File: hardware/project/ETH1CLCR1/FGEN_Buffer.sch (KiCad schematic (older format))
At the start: 37 parts, among them K1201 UMS05-1A80-75D, K1202 UMS05-1A80-75D, K1203 UMS05-1A80-75D, K1204 UMS05-1A80-75D, Q1201 MMBT4401L, Q1202 MMBT4403L, U1201 LT1468

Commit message: Schematic design
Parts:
- added C1205, C1206, C1207, C1208: 100n, symbol Device:C
- added C1209: C, symbol Device:C
- added R1219, R1220: R, symbol Device:R
- added U1202: TL072, symbol Amplifier_Operational:TL072
- gave numbers to parts that had none: 18
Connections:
- net +15VF: now also C1205.1, C1206.1, U1202.8 (V+)
- net -15VF: now also C1207.1, C1208.1, U1202.4 (V-)
- net AGNDF: now also C1205.2, C1206.2, C1207.2, C1208.2, U1202.3 (+), U1202.5 (+)
- net FGEN: now reaches U1201.3 (+)
- net at R1204.1, R1206.1, R1213.1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: now also R1219.2, U1202.2 (-)
- net SR10KCTR: now reaches R1209.1
- net SR1KCTR: now reaches R1210.1
- net SR100CTR: now reaches R1211.1
- net SR10CTR: now reaches R1212.1
- new net: C1209.2, R1219.1, U1202.1
- new net: C1209.1, R1220.2, U1202.6 (-)
- new net: R1220.1, U1202.7
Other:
- moved on the sheet: C1201, C1202, C1203, C1204, D1201, D1202, D1203, D1204, K1201A, K1201B, K1202A, K1202B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

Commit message: Schematic design
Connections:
- net +15VF renamed +12VF
- net -15VF renamed -12VF
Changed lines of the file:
@@
 Wire Wire Line
 	4700 3000 5400 3000
-$Comp
-L ETH1CLCR1:+15VF #PWR01201
-U 1 1 5E34A40C
-P 4750 2000
-F 0 "#PWR01201" H 4750 1850 50  0001 C CNN
-F 1 "+15VF" V 4765 2128 50  0000 L CNN
-F 2 "" H 4750 2000 50  0001 C CNN
-F 3 "" H 4750 2000 50  0001 C CNN
-	1    4750 2000
-	0    1    1    0
-$EndComp
 Wire Wire Line
 	4750 2000 4700 2000
 Connection ~ 4700 2000
-$Comp
-L ETH1CLCR1:-15VF #PWR01205
-U 1 1 5E34C013
-P 4750 4000
-F 0 "#PWR01205" H 4750 3850 50  0001 C CNN
-F 1 "-15VF" V 4765 4128 50  0000 L CNN
-F 2 "" H 4750 4000 50  0001 C CNN
-F 3 "" H 4750 4000 50  0001 C CNN
-	1    4750 4000
-	0    1    1    0
-$EndComp
 Wire Wire Line
 	4750 4000 4700 4000
@@
 	1    0    0    -1
 $EndComp
-$Comp
-L ETH1CLCR1:+15VF #PWR?
-U 1 1 5E371215
-P 3550 2600
-AR Path="/5DEEF70B/5E371215" Ref="#PWR?"  Part="1"
-AR Path="/5E314C16/5E371215" Ref="#PWR01202"  Part="1"
-F 0 "#PWR01202" H 3550 2450 50  0001 C CNN
-F 1 "+15VF" H 3565 2773 50  0000 C CNN
-F 2 "" H 3550 2600 50  0001 C CNN
-F 3 "" H 3550 2600 50  0001 C CNN
-	1    3550 2600
-	1    0    0    -1
-$EndComp
-$Comp
-L ETH1CLCR1:-15VF #PWR?
-U 1 1 5E37121B
-P 3550 3400
-AR Path="/5DEEF70B/5E37121B" Ref="#PWR?"  Part="1"
-AR Path="/5E314C16/5E37121B" Ref="#PWR01203"  Part="1"
-F 0 "#PWR01203" H 3550 3250 50  0001 C CNN
-F 1 "-15VF" H 3565 3573 50  0000 C CNN
-F 2 "" H 3550 3400 50  0001 C CNN
-F 3 "" H 3550 3400 50  0001 C CNN
-	1    3550 3400
-	-1   0    0    1
-$EndComp
 NoConn ~ 3650 3350
 NoConn ~ 3750 3300
@@
 	1    0    0    -1
 $EndComp
-$Comp
-L ETH1CLCR1:+15VF #PWR01215
-U 1 1 5E007FE3
-P 4500 6650
-F 0 "#PWR01215" H 4500 6500 50  0001 C CNN
-F 1 "+15VF" H 4515 6823 50  0000 C CNN
-F 2 "" H 4500 6650 50  0001 C CNN
-F 3 "" H 4500 6650 50  0001 C CNN
-	1    4500 6650
-	1    0    0    -1
-$EndComp
-$Comp
-L ETH1CLCR1:-15VF #PWR01216
-U 1 1 5E008AEC
-P 4500 7250
-F 0 "#PWR01216" H 4500 7100 50  0001 C CNN
-F 1 "-15VF" H 4515 7423 50  0000 C CNN
-F 2 "" H 4500 7250 50  0001 C CNN
-F 3 "" H 4500 7250 50  0001 C CNN
-	1    4500 7250
-	-1   0    0    1
-$EndComp
 Wire Wire Line
 	7850 2300 7800 2300
@@
 $EndComp
 $Comp
-L ETH1CLCR1:+15VF #PWR01217
-U 1 1 5E0853A4
-P 5050 6650
-F 0 "#PWR01217" H 5050 6500 50  0001 C CNN
-F 1 "+15VF" H 5065 6823 50  0000 C CNN
-F 2 "" H 5050 6650 50  0001 C CNN
-F 3 "" H 5050 6650 50  0001 C CNN
-	1    5050 6650
-	1    0    0    -1
-$EndComp
-$Comp
 L ETH1CLCR1:AGNDF #PWR01218
 U 1 1 5E085ACE
@@
 $EndComp
 $Comp
-L ETH1CLCR1:+15VF #PWR01219
-U 1 1 5E096A26
-P 5550 6650
-F 0 "#PWR01219" H 5550 6500 50  0001 C CNN
-F 1 "+15VF" H 5565 6823 50  0000 C CNN
-F 2 "" H 5550 6650 50  0001 C CNN
-F 3 "" H 5550 6650 50  0001 C CNN
-	1    5550 6650
-	1    0    0    -1
-$EndComp
-$Comp
 L ETH1CLCR1:AGNDF #PWR01220
 U 1 1 5E096A2C
@@
 	6550 6800 6550 6650
 $Comp
-L ETH1CLCR1:-15VF #PWR01221
-U 1 1 5E0B05E8
+L ETH1CLCR1:+12VF #PWR?
+U 1 1 5E56817A
+P 4750 2000
+F 0 "#PWR?" H 4750 1850 50  0001 C CNN
+F 1 "+12VF" V 4765 2128 50  0000 L CNN
+F 2 "" H 4750 2000 50  0001 C CNN
+F 3 "" H 4750 2000 50  0001 C CNN
+	1    4750 2000
+	0    1    1    0
+$EndComp
+$Comp
+L ETH1CLCR1:+12VF #PWR?
+U 1 1 5E5690F9
+P 3550 2600
+F 0 "#PWR?" H 3550 2450 50  0001 C CNN
+F 1 "+12VF" H 3565 2773 50  0000 C CNN
+F 2 "" H 3550 2600 50  0001 C CNN
+F 3 "" H 3550 2600 50  0001 C CNN
+	1    3550 2600
+	1    0    0    -1
+$EndComp
+$Comp
+L ETH1CLCR1:-12VF #PWR?
+U 1 1 5E56BEE2
+P 4750 4000
+F 0 "#PWR?" H 4750 3850 50  0001 C CNN
+F 1 "-12VF" V 4765 4128 50  0000 L CNN
+F 2 "" H 4750 4000 50  0001 C CNN
+F 3 "" H 4750 4000 50  0001 C CNN
+	1    4750 4000
+	0    1    1    0
+$EndComp
+$Comp
+L ETH1CLCR1:-12VF #PWR?
+U 1 1 5E570823
+P 6550 6650
+F 0 "#PWR?" H 6550 6500 50  0001 C CNN
+F 1 "-12VF" H 6565 6823 50  0000 C CNN
+F 2 "" H 6550 6650 50  0001 C CNN
+F 3 "" H 6550 6650 50  0001 C CNN
+	1    6550 6650
+	1    0    0    -1
+$EndComp
+$Comp
+L ETH1CLCR1:-12VF #PWR?
+U 1 1 5E570ACC
 P 6050 6650
-F 0 "#PWR01221" H 6050 6500 50  0001 C CNN
-F 1 "-15VF" H 6065 6823 50  0000 C CNN
+F 0 "#PWR?" H 6050 6500 50  0001 C CNN
+F 1 "-12VF" H 6065 6823 50  0000 C CNN
 F 2 "" H 6050 6650 50  0001 C CNN
 F 3 "" H 6050 6650 50  0001 C CNN
@@
 $EndComp
 $Comp
-L ETH1CLCR1:-15VF #PWR01223
-U 1 1 5E0B0E84
-P 6550 6650
-F 0 "#PWR01223" H 6550 6500 50  0001 C CNN
-F 1 "-15VF" H 6565 6823 50  0000 C CNN
-F 2 "" H 6550 6650 50  0001 C CNN
-F 3 "" H 6550 6650 50  0001 C CNN
-	1    6550 6650
-	1    0    0    -1
+L ETH1CLCR1:+12VF #PWR?
+U 1 1 5E5712DC
+P 5550 6650
+F 0 "#PWR?" H 5550 6500 50  0001 C CNN
+F 1 "+12VF" H 5565 6823 50  0000 C CNN
+F 2 "" H 5550 6650 50  0001 C CNN
+F 3 "" H 5550 6650 50  0001 C CNN
+	1    5550 6650
+	1    0    0    -1
+$EndComp
+$Comp
+L ETH1CLCR1:+12VF #PWR?
+U 1 1 5E5716B1
+P 5050 6650
+F 0 "#PWR?" H 5050 6500 50  0001 C CNN
+F 1 "+12VF" H 5065 6823 50  0000 C CNN
+F 2 "" H 5050 6650 50  0001 C CNN
+F 3 "" H 5050 6650 50  0001 C CNN
+	1    5050 6650
+	1    0    0    -1
+$EndComp
+$Comp
+L ETH1CLCR1:+12VF #PWR?
+U 1 1 5E5719C0
+P 4500 6650
+F 0 "#PWR?" H 4500 6500 50  0001 C CNN
+F 1 "+12VF" H 4515 6823 50  0000 C CNN
+F 2 "" H 4500 6650 50  0001 C CNN
+F 3 "" H 4500 6650 50  0001 C CNN
+	1    4500 6650
+	1    0    0    -1
+$EndComp
+$Comp
+L ETH1CLCR1:-12VF #PWR?
+U 1 1 5E571D8E
+P 4500 7250
+F 0 "#PWR?" H 4500 7100 50  0001 C CNN
+F 1 "-12VF" H 4515 7423 50  0000 C CNN
+F 2 "" H 4500 7250 50  0001 C CNN
+F 3 "" H 4500 7250 50  0001 C CNN
+	1    4500 7250
+	-1   0    0    1
+$EndComp
+$Comp
+L ETH1CLCR1:-12VF #PWR?
+U 1 1 5E579016
+P 3550 3400
+F 0 "#PWR?" H 3550 3250 50  0001 C CNN
+F 1 "-12VF" H 3565 3573 50  0000 C CNN
+F 2 "" H 3550 3400 50  0001 C CNN
+F 3 "" H 3550 3400 50  0001 C CNN
+	1    3550 3400
+	-1   0    0    1
 $EndComp
 $EndSCHEMATC

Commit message: Schematic design
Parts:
- removed R1220: R, symbol Device:R
- removed U1201: LT1468, Package_SO:SSOP-8_3.9x5.05mm_P1.27mm, symbol ETH1CLCR1:LT1468
- added C1101: 1u, symbol Device:C
- added C1102: 220u, symbol Device:CP
- added R1101: 1k, Resistor_SMD:R_0603_1608Metric_Pad1.05x0.95mm_HandSolder, symbol Device:R
- added R1102: 0, Resistor_SMD:R_0603_1608Metric_Pad1.05x0.95mm_HandSolder, symbol Device:R
- added R1103: 550, Resistor_SMD:R_0603_1608Metric_Pad1.05x0.95mm_HandSolder, symbol Device:R
- added RV1101: 500, Resistor_SMD:R_0603_1608Metric_Pad1.05x0.95mm_HandSolder, symbol Device:R_POT_TRIM
- added U1101: RC4558, symbol Amplifier_Operational:RC4558
- added U1102: AD5293BRUZ-20, Package_SO:TSSOP-14_4.4x5mm_P0.65mm, symbol Potentiometer_Digital:AD5293
- C1201, C1202, C1203, C1204, C1205, C1206, C1207, C1208: footprint (none) -> Capacitor_SMD:C_0603_1608Metric_Pad1.05x0.95mm_HandSolder
- C1209: value C -> 43p; footprint (none) -> Capacitor_SMD:C_0603_1608Metric_Pad1.05x0.95mm_HandSolder
- D1201, D1202: value D -> 1N4149
- D1203, D1204: value D_Zener -> 54V
- R1201, R1202, R1206, R1207, R1208, R1213, R1218: footprint (none) -> Resistor_SMD:R_0603_1608Metric_Pad1.05x0.95mm_HandSolder
- R1203, R1205: value 27 -> 27/1W
- R1209, R1210, R1211, R1212: value R -> 10k; footprint (none) -> Resistor_SMD:R_0603_1608Metric_Pad1.05x0.95mm_HandSolder
- R1214: value R -> 200; footprint (none) -> Resistor_SMD:R_0603_1608Metric_Pad1.05x0.95mm_HandSolder
- R1215: value 100 -> 200; footprint (none) -> Resistor_SMD:R_0603_1608Metric_Pad1.05x0.95mm_HandSolder
- R1216: value R -> 2k; footprint (none) -> Resistor_SMD:R_0603_1608Metric_Pad1.05x0.95mm_HandSolder
- R1217: value 1k -> 2k; footprint (none) -> Resistor_SMD:R_0603_1608Metric_Pad1.05x0.95mm_HandSolder
- R1219: value R -> 205; footprint (none) -> Resistor_SMD:R_0603_1608Metric_Pad1.05x0.95mm_HandSolder
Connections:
- net +12VF: now also U1101.8 (V+)
- net -12VF: now also U1101.4 (V-)
- net AGNDF: now also C1101.2, U1101.5 (+), U1102.9 (GND)
- net FGEN: now also U1101.3 (+)
- net HCUR: now reaches R1204.1, R1206.1, R1213.1, R1214.1, R1215.1, R1216.1, R1217.1, R1218.1, R1219.2, U1202.2 (-)
- net TRIM_3: now reaches C1209.1, U1202.6 (-)
- net TRIM_3: now also R1103.2, RV1101.3, U1102.3 (RH)
- net VLI: now reaches U1202.7
- net VLI: now also R1103.1, RV1101.2, U1102.4 (RW)
- net at K1201.3, K1202.3, K1203.3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: now also C1102.2, R1102.1; no longer R1201.1, R1203.2, R1205.1
- net at D1201.1 (K), D1202.2 (A): now also U1101.1
- net at R1201.2, R1207.1: now also U1101.2 (-)
- new net: U1101.6 (-), U1101.7
- new net: C1101.1, U1102.7 (EXT_CAP)
- new net: C1102.1, R1102.2, R1201.1, R1203.2, R1205.1
- new net +15VF: U1102.6 (Vdd+)
- new net +3.3VF: R1101.1, U1102.8 (Vlog)
- new net -15VF: U1102.2 (Vss-)
- new net FB_CLK: U1102.11 (CLK)
- new net FB_RDY: R1101.2, U1102.14 (RDY)
- new net FB_SDI: U1102.10 (SDI)
- new net FB_SDO: U1102.13 (SDO)
- new net FB_~CS: U1102.12 (~CS~)
- new net FB_~RST: U1102.1 (~RST~)
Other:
- moved on the sheet: C1209, D1201, D1202, D1203, D1204, K1201A, K1202A, K1203A, K1204A, Q1201, Q1202, R1201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

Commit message: Need to redesign the AC source, the LT1468 is too slow.
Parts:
- D1201, D1202: footprint (none) -> Diode_SMD:D_SOD-123
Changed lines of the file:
@@
 F 0 "D1201" V 3646 2921 50  0000 R CNN
 F 1 "1N4149" V 3555 2921 50  0000 R CNN
-F 2 "" H 3600 3000 50  0001 C CNN
+F 2 "Diode_SMD:D_SOD-123" H 3600 3000 50  0001 C CNN
 F 3 "~" H 3600 3000 50  0001 C CNN
 	1    3600 3000
@@
 F 0 "D1202" V 3646 3321 50  0000 R CNN
 F 1 "1N4149" V 3555 3321 50  0000 R CNN
-F 2 "" H 3600 3400 50  0001 C CNN
+F 2 "Diode_SMD:D_SOD-123" H 3600 3400 50  0001 C CNN
 F 3 "~" H 3600 3400 50  0001 C CNN
 	1    3600 3400

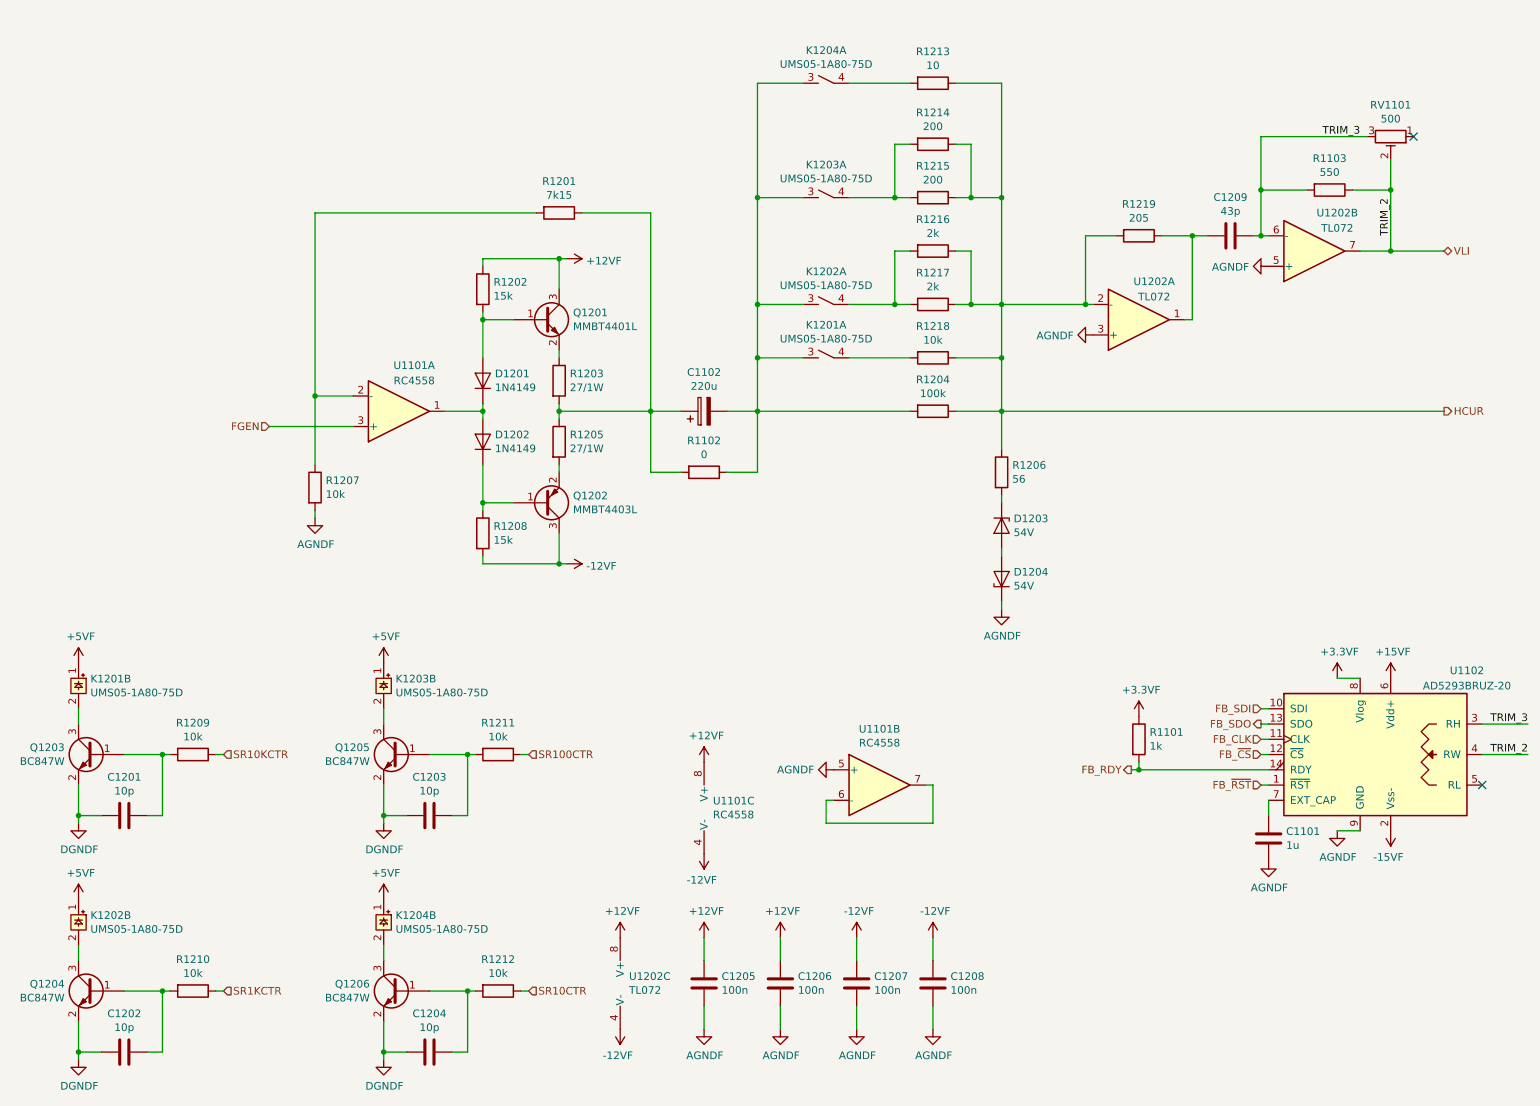
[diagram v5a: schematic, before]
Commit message: Footprint asigment (not finished).
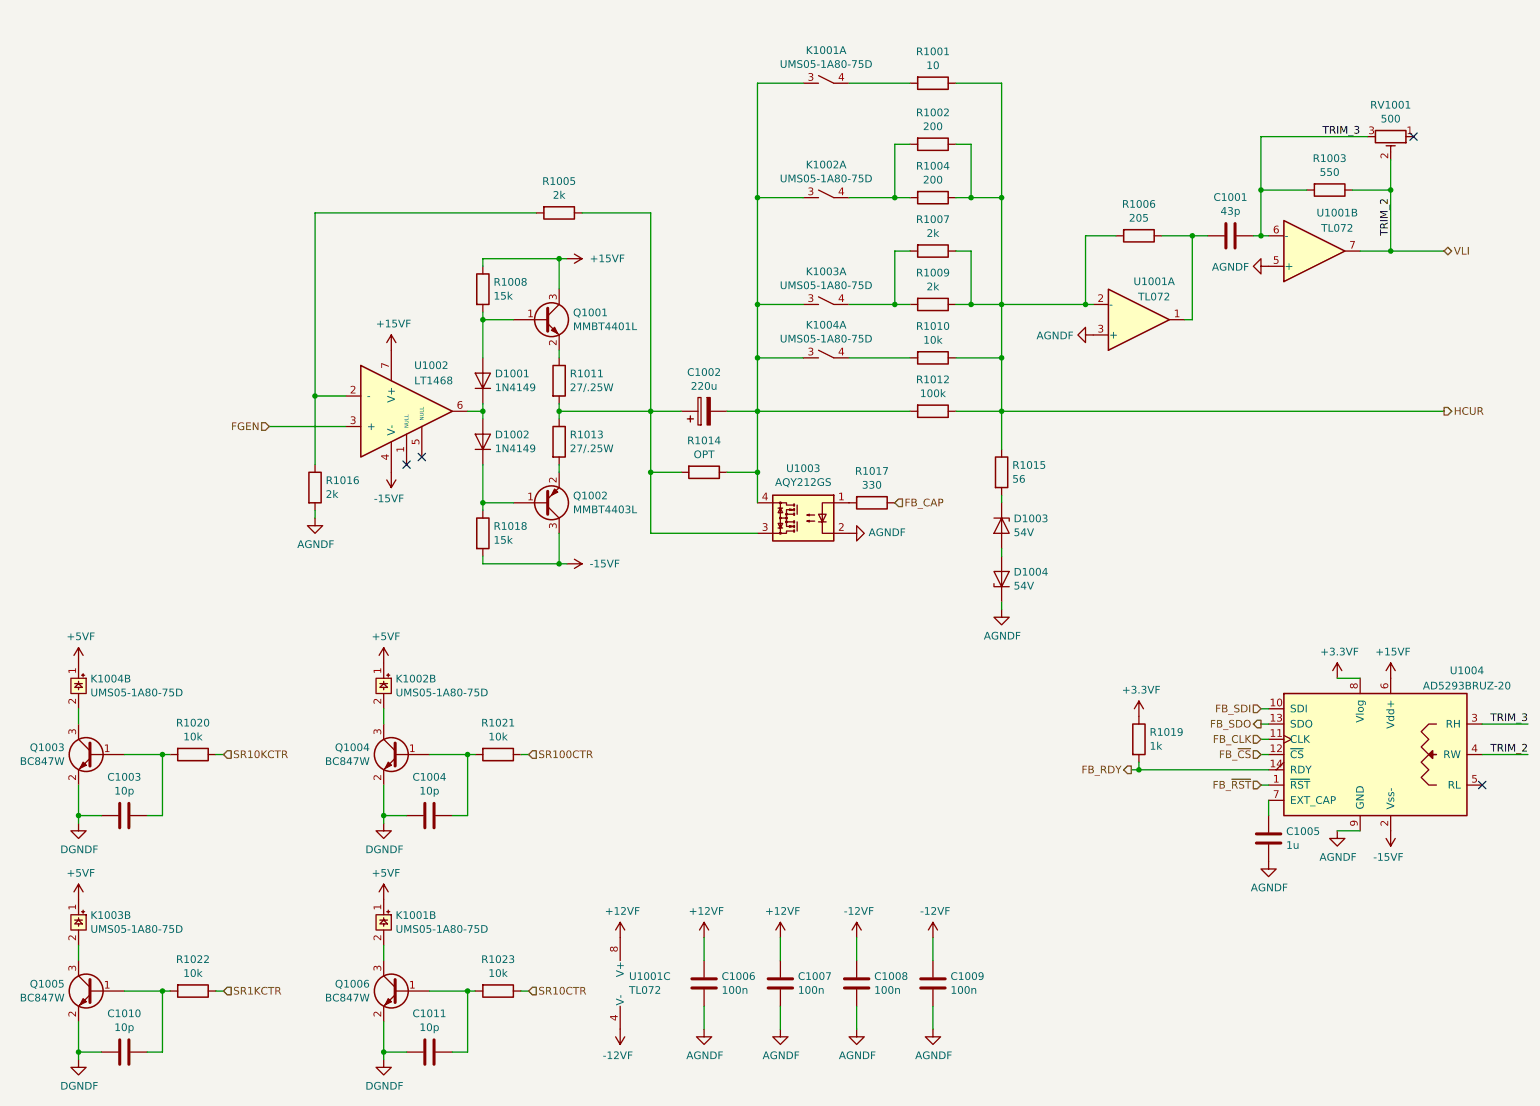
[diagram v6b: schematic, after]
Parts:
- removed U1101: RC4558, symbol Amplifier_Operational:RC4558
- added R1017: 330, Resistor_SMD:R_0603_1608Metric_Pad1.05x0.95mm_HandSolder, symbol Device:R
- added U1002: LT1468, Package_SO:SSOP-8_3.9x5.05mm_P1.27mm, symbol ETH1CLCR1:LT1468
- added U1003: AQY212GS, ETH1CLCR1:AQY212GS, symbol ETH1CLCR1:AQY212GS
- C1005: renamed from C1101; footprint (none) -> Capacitor_SMD:C_0805_2012Metric_Pad1.15x1.40mm_HandSolder
- Q1001: renamed from Q1201; footprint (none) -> Package_TO_SOT_SMD:SOT-23
- Q1002: renamed from Q1202; footprint (none) -> Package_TO_SOT_SMD:SOT-23
- R1005: renamed from R1201; value 7k15 -> 2k
- R1011: renamed from R1203; value 27/1W -> 27/.25W
- R1012: renamed from R1204; footprint (none) -> Resistor_SMD:R_0603_1608Metric_Pad1.05x0.95mm_HandSolder
- R1013: renamed from R1205; value 27/1W -> 27/.25W
- R1014: renamed from R1102; value 0 -> OPT
- R1016: renamed from R1207; value 10k -> 2k
- U1001: renamed from U1202; footprint (none) -> Package_SO:SOIC-8_3.9x4.9mm_P1.27mm
- renumbered C1209 to C1001, C1102 to C1002, C1201 to C1003, C1203 to C1004, C1205 to C1006, C1206 to C1007, C1207 to C1008, C1208 to C1009, C1202 to C1010, C1204 to C1011, D1201 to D1001, D1202 to D1002, D1203 to D1003, D1204 to D1004, K1204 to K1001, K1203 to K1002, K1202 to K1003, K1201 to K1004, Q1203 to Q1003, Q1205 to Q1004, Q1204 to Q1005, Q1206 to Q1006, R1213 to R1001, R1214 to R1002, R1103 to R1003, R1215 to R1004, R1219 to R1006, R1216 to R1007, R1202 to R1008, R1217 to R1009, R1218 to R1010, R1206 to R1015, R1208 to R1018, R1101 to R1019, R1209 to R1020, R1211 to R1021, R1210 to R1022, R1212 to R1023, RV1101 to RV1001, U1102 to U1004
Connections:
- net +12VF: no longer Q1001.3 (C), R1008.1
- net +15VF: now also Q1001.3 (C), R1008.1, U1002.7 (V+)
- net -12VF: no longer Q1002.3 (C), R1018.2
- net -15VF: now also Q1002.3 (C), R1018.2, U1002.4 (V-)
- net AGNDF: now also U1003.2
- net FGEN: now also U1002.3 (+)
- net at D1001.1 (K), D1002.2 (A): now also U1002.6
- net at R1005.2, R1016.1: now also U1002.2 (-)
- net at C1002.2, K1001.3, K1002.3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: now also U1003.4
- net at C1002.1, R1005.1, R1011.2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: now also U1003.3
- new net: R1017.2, U1003.1
- new net FB_CAP: R1017.1
- no-connect marks 2 -> 4

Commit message: Modification in schematic and PCB layout.
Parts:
- removed K1001, K1002, K1003, K1004: UMS05-1A80-75D, symbol ETH1CLCR1:UMS05-1A80-75D
- added D1005, D1006, D1007, D1008: 1N4148, Diode_SMD:D_SOD-123, symbol Device:D
- added K1001, K1002, K1003, K1004: 9012, ETH1CLCR1:9012, symbol ETH1CLCR1:9012
- C1002: value 220u -> EEHZC1V221V; footprint (none) -> Capacitor_SMD:CP_Elec_10x10
- C1005: footprint Capacitor_SMD:C_0805_2012Metric_Pad1.15x1.40mm_HandSolder -> Capacitor_SMD:C_0603_1608Metric_Pad1.05x0.95mm_HandSolder
- D1003, D1004: value 54V -> SML4757A; footprint (none) -> Diode_SMD:D_SMA_Handsoldering
- R1011, R1013: footprint (none) -> Resistor_SMD:R_0805_2012Metric_Pad1.15x1.40mm_HandSolder
- RV1001: value 500 -> 3314J-1-501E; footprint Resistor_SMD:R_0603_1608Metric_Pad1.05x0.95mm_HandSolder -> Potentiometer_SMD:Potentiometer_Bourns_3314J_Vertical
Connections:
- net +5VF: now also D1005.1 (K), D1006.1 (K), D1007.1 (K), D1008.1 (K), K1001.2, K1002.2, K1003.2, K1004.2
- net at C1002.2, R1012.2, R1014.1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: now also K1001.1, K1002.1, K1003.1, K1004.1
- net at R1007.2, R1009.2: now also K1003.4
- net at Q1005.3 (C): now also D1006.2 (A), K1003.3
- net at R1002.2, R1004.2: now also K1002.4
- net at Q1004.3 (C): now also D1007.2 (A), K1002.3
- net at R1001.2: now also K1001.4
- net at Q1006.3 (C): now also D1008.2 (A), K1004.3
- net at R1010.2: now also K1004.4
- net at Q1003.3 (C): now also D1005.2 (A), K1001.3
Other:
- moved on the sheet: C1003, C1004, Q1003, Q1004, R1020, R1021
